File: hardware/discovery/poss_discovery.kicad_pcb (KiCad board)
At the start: 2 copper layers, 96.5 x 66 mm, 56 parts, among them J1 HEADER_2, J2 HEADER_25x2, J3 HEADER_25x2, J5 HEADER_2, SW1 SW_PUSH, SW10 SW_PUSH, SW11 SW_PUSH, SW12 SW_PUSH, SW13 SW_PUSH, SW14 SW_PUSH, SW15 SW_PUSH, SW16 SW_PUSH, SW17 SW_PUSH, SW18 SW_PUSH, SW19 SW_PUSH, SW2 SW_PUSH, SW20 SW_PUSH, SW21 SW_PUSH, SW22 SW_PUSH, SW3 SW_PUSH, SW4 SW_PUSH, SW5 SW_PUSH, SW6 SW_PUSH, SW7 SW_PUSH, SW8 SW_PUSH, SW9 SW_PUSH

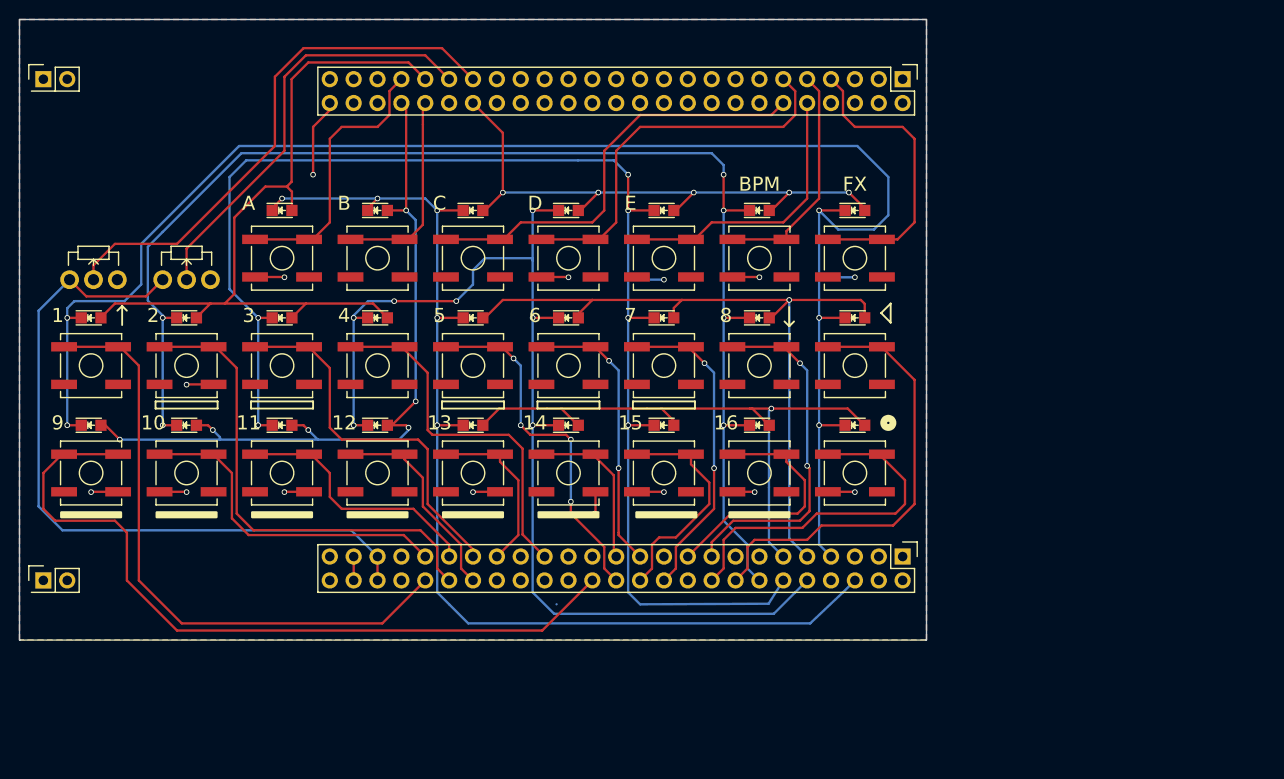
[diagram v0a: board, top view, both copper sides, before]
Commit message: Start RevB of the discovery board
- Fix RevA known problems
- Custom scheme and footprint for the headers
- Improved silkscreen
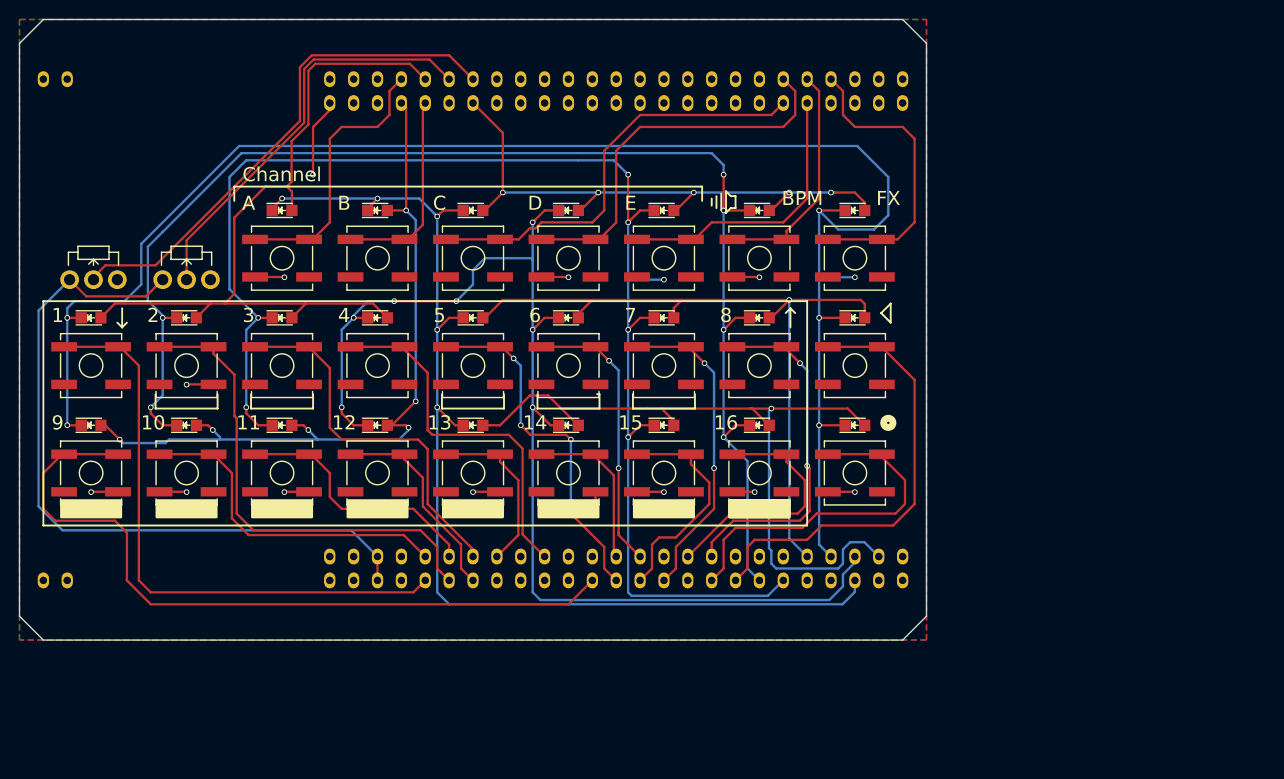
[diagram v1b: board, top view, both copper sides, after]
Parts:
- removed J1, J5: HEADER_2, Pin_Headers:Pin_Header_Straight_2x01
- removed J2, J3: HEADER_25x2, Pin_Headers:Pin_Header_Straight_2x25
- added U1: STM32F4_DISCO_Header, stm32f4-disco:STM32F4-DISCO-HEADERS-TH, B.Cu at (80.0, 95.2)
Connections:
- net /3V renamed 3V
- net /COL1 renamed COL1
- net /COL2 renamed COL2
- net /COL3 renamed COL3
- net /COL4 renamed COL4
- net /COL5 renamed COL5
- net /GND renamed GND
- net /PA13 renamed ROW2
- net /PA15 renamed ROW3
- net /PA8 renamed ROW5
- net /PC11 renamed ROW4
- net /PC9 renamed ROW1
- Play1 pad 1: /PD0 -> Play
- Play2 pad 1: /FX -> FX
- RV1 pad 2: /PA1 -> POT1
- RV2 pad 2: /PA3 -> POT2
- SW1 pad 1: /B1 -> B1
- SW10 pad 1: /B10 -> B10
- SW11 pad 1: /B11 -> B11
- SW12 pad 1: /B12 -> B12
- SW13 pad 1: /B13 -> B13
- SW14 pad 1: /B14 -> B14
- SW15 pad 1: /B15 -> B15
- SW16 pad 1: /B16 -> B16
- SW17 pad 1: /BF1 -> BA
- SW18 pad 1: /BF2 -> BB
- SW19 pad 1: /BF3 -> BC
- SW2 pad 1: /B2 -> B2
- SW20 pad 1: /BF4 -> BD
- SW21 pad 1: /BF5 -> BE
- SW22 pad 1: /BPM -> BPM_VOL
- SW3 pad 1: /B3 -> B3
- SW4 pad 1: /B4 -> B4
- SW5 pad 1: /B5 -> B5
- SW6 pad 1: /B6 -> B6
- SW7 pad 1: /B7 -> B7
- SW8 pad 1: /B8 -> B8
- SW9 pad 1: /B9 -> B9
- Write1 pad 1: /PD2 -> Write
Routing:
- net /B9: track 81.6 -> 0.00 mm
- net B9: track 0.00 -> 79.2 mm
- net /B1: track 65.9 -> 0.00 mm
- net B1: track 0.00 -> 63.2 mm
- net /PA3: track 57.2 -> 0.00 mm
- net POT2: track 0.00 -> 54.8 mm
- net /B2: track 51.5 -> 0.00 mm
- net B2: track 0.00 -> 51.4 mm
- net Play: track 0.00 -> 47.7 mm
- net /PD0: track 47.7 -> 0.00 mm
- net /BF3: track 45.6 -> 0.00 mm
- net /PA1: track 45.4 -> 0.00 mm
- net POT1: track 0.00 -> 44.3 mm
- net /BF4: track 41.3 -> 0.00 mm
- net B3: track 0.00 -> 40.3 mm
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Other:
- outline, holes or cut-outs redrawn
- board text added: "Channel"
- board text added: "RevB"

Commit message: Discovery: Start power section
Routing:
- net GND: track 42.0 -> 33.6 mm, vias 13 -> 12
- net ROW2: track 125.6 -> 124.2 mm
- net COL3: track 62.3 -> 63.5 mm
- net COL2: track 78.9 -> 79.6 mm

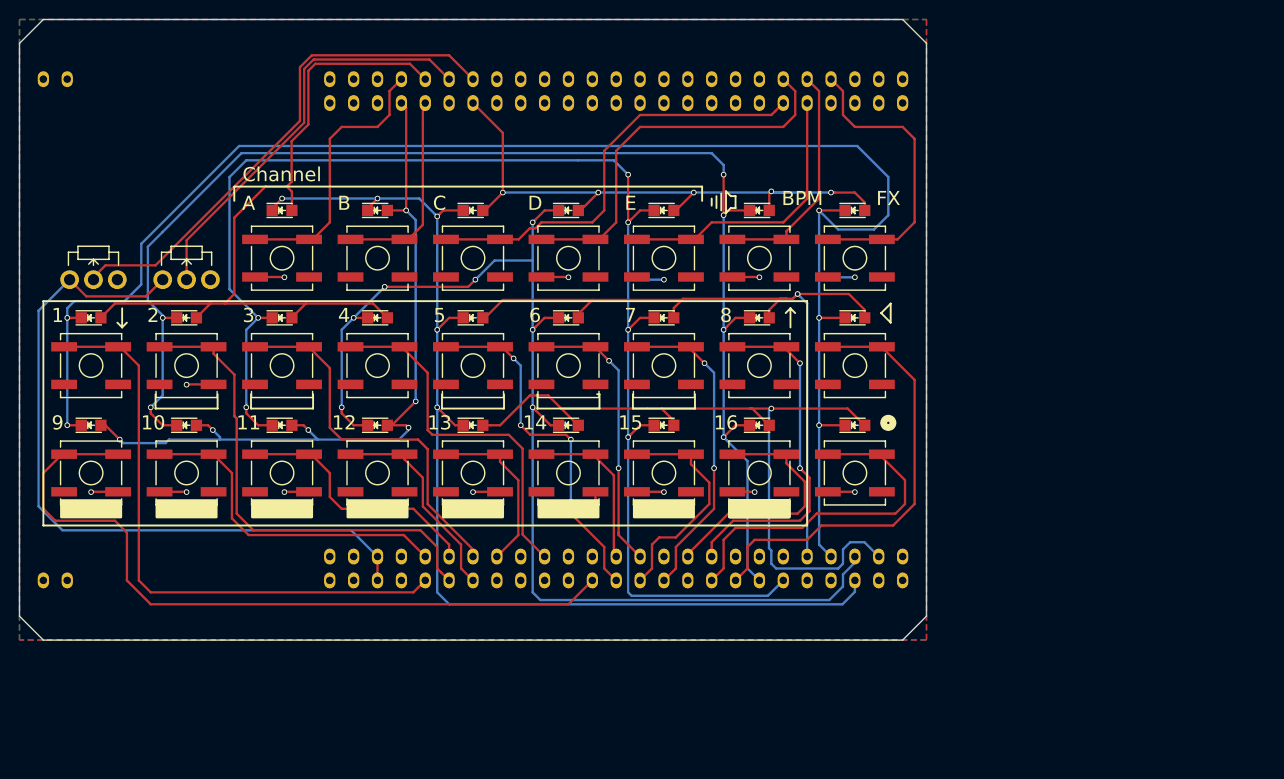
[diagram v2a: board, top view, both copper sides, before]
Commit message: Discovery: add the MCU
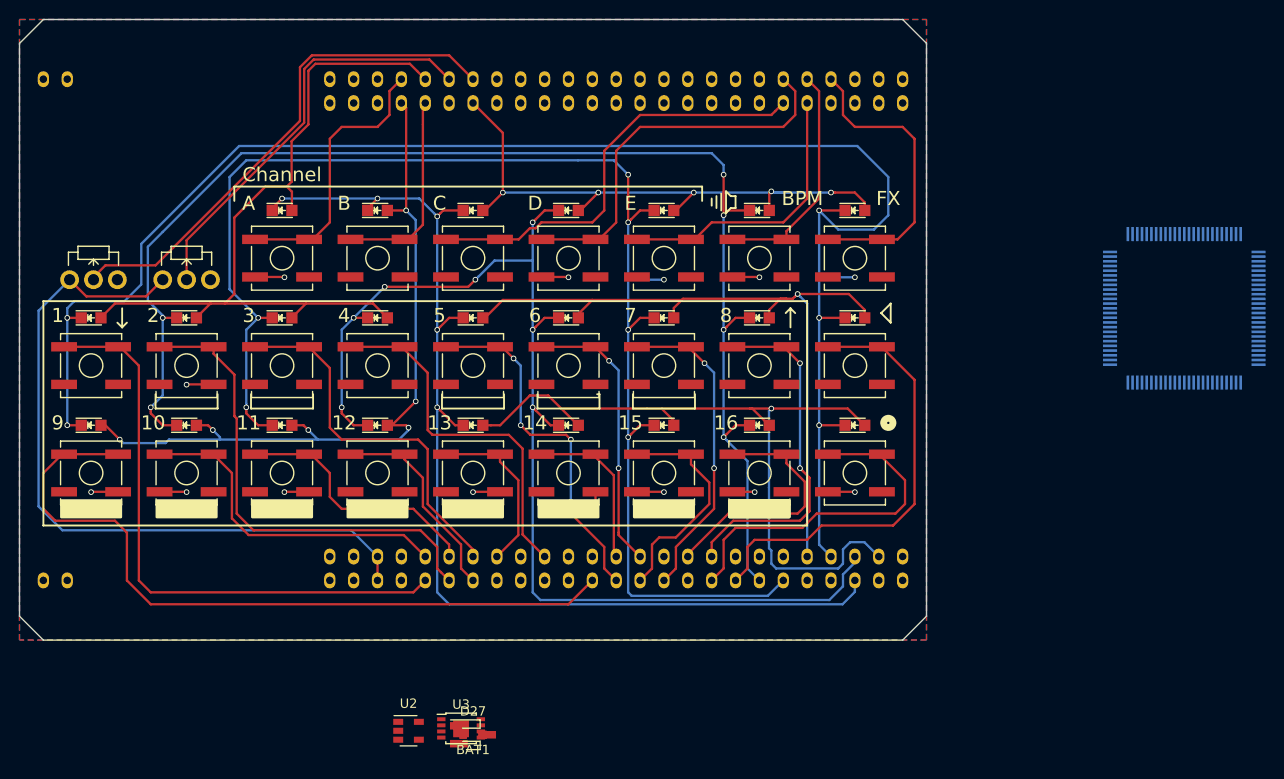
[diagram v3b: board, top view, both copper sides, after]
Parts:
- added BAT1: LED, Diodes_SMD:D_0805, F.Cu at (128.3, 154.9)
- added D27: DOUBLE_SCH_KCOM, TO_SOT_Packages_SMD:SOT-23_Handsoldering, F.Cu at (128.3, 154.9)
- added U2: MCP73831, TO_SOT_Packages_SMD:SOT-23-5, F.Cu at (121.4, 154.4)
- added U3: BD33IA5, Housings_SSOP:MSOP-8-1EP_3x3mm_Pitch0.65mm, F.Cu at (127.0, 154.2)
- added U4: STM32F407VG, Housings_QFP:LQFP-100_14x14mm_Pitch0.5mm, B.Cu at (204.0, 109.5)
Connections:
- net 3V renamed 3V3
- U1 pad 74: SWDCLK -> SWCLK

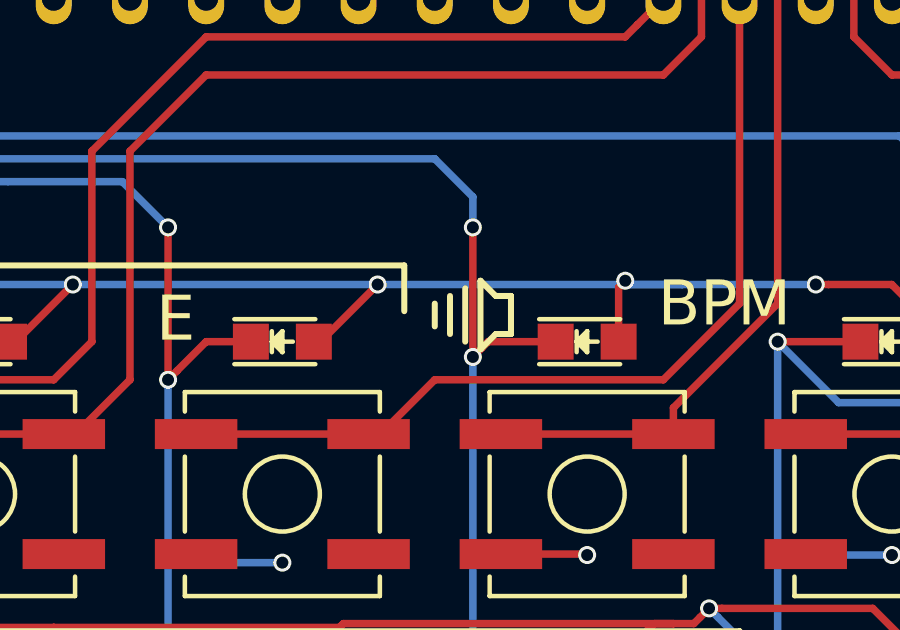
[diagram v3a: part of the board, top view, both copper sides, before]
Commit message: Discovery: Fix volume symbol
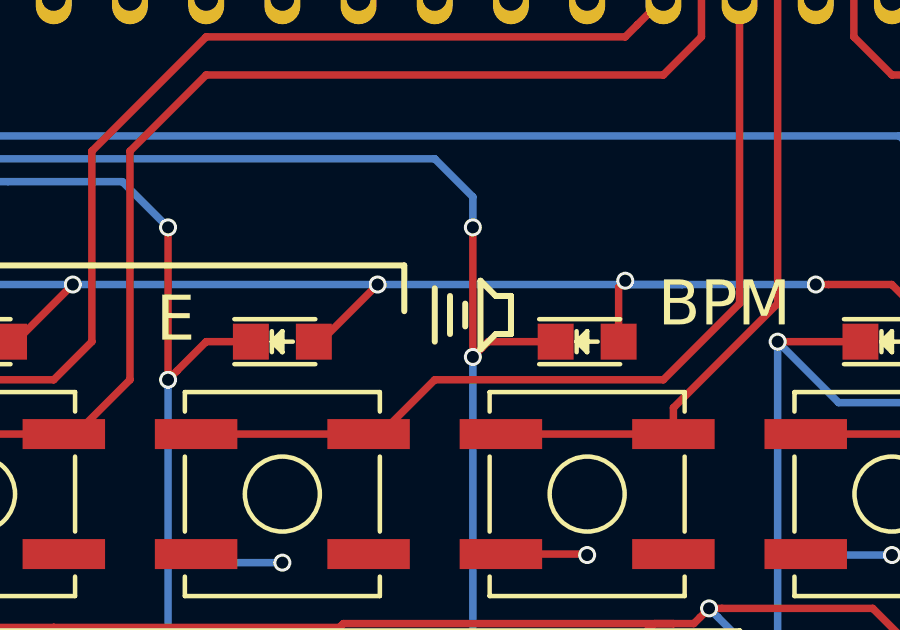
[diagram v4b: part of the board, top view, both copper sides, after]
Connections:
- U1 pad 22: BF4 -> BD
- U1 pad 32: BF2 -> BB
- U1 pad 47: BF3 -> BC
- U1 pad 48: BF5 -> BE
- U1 pad 6: BF1 -> BA
- U4 pad 16: BF1 -> BA
- U4 pad 17: BF2 -> BB
- U4 pad 54: BF4 -> BD
- U4 pad 55: BF3 -> BC
- U4 pad 57: BF5 -> BE
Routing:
- net BF3: track 37.9 -> 0.00 mm
- net BC: track 7.74 -> 45.6 mm
- net BF4: track 32.6 -> 0.00 mm
- net BD: track 8.70 -> 41.3 mm
- net BF5: track 21.4 -> 0.00 mm
- net BE: track 8.70 -> 30.1 mm
- net BF1: track 20.6 -> 0.00 mm
- net BA: track 8.70 -> 29.3 mm
- net BF2: track 13.1 -> 0.00 mm
- net BB: track 8.35 -> 21.4 mm

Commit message: Discovery start power section
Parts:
- added ?: tempo_logo, stm32f4-disco:tempo_logo, F.Cu at (162.1, 103.4)
- added BT1: BATTERY, Connect:PINHEAD1-2, F.Cu at (106.8, 83.9)
- added C1: 10uF, Capacitors_SMD:C_0805, F.Cu at (116.6, 81.4)
- added C2: 4.7uF, Capacitors_SMD:C_0805, F.Cu at (140.4, 83.2)
- added C3: 47uF, Capacitors_SMD:C_1206, F.Cu at (149.5, 83.3)
- added CON1: USB-MICRO-B, Connect:USB_Micro-B, F.Cu at (128.8, 83.3)
- added R1: 1K, Resistors_SMD:R_0805, F.Cu at (119.8, 84.3)
- added R2: 10K, Resistors_SMD:R_0805, F.Cu at (112.9, 84.5)
- D27: value DOUBLE_SCH_KCOM -> DOUBLE_SCH_KCOM_PMEG2005CT; footprint TO_SOT_Packages_SMD:SOT-23_Handsoldering -> TO_SOT_Packages_SMD:SOT-23
- U1: footprint stm32f4-disco:STM32F4-DISCO-HEADERS-TH -> stm32f4-disco:STM32F4-DISCO-HEADERS-SMD
- U4: moved to F.Cu
- moved U3 73.1 mm to (144.8, 83.2), turned to 180 degrees
- moved BAT1 71.0 mm to (121.8, 84.2), turned to 90 degrees
- moved U2 70.3 mm to (116.6, 84.3), turned to 180 degrees
- moved D27 66.8 mm to (128.8, 88.0), turned to 270 degrees
- moved U4 47.5 mm to (160.0, 91.4)
- moved U1 28.2 mm to (108.0, 91.4)
- moved D21 19.1 mm to (117.9, 118.1)
- moved D10 7.62 mm to (168.9, 118.1)
- moved D11 7.62 mm to (128.3, 106.7)
- moved D12 7.62 mm to (138.4, 106.7)
- moved D13 7.62 mm to (148.6, 106.7)
- moved D14 7.62 mm to (158.8, 106.7)
- moved D15 7.62 mm to (168.9, 106.7)
- moved D16 7.62 mm to (108.0, 106.7)
- moved D18 7.62 mm to (108.0, 118.1)
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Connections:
- D27 pad 1: VBAT -> VBUS
- D27 pad 2: VIN -> VBAT
- D27 pad 3: VBUS -> VIN
- U4 pad 70: Net-(U4-Pad70) -> FS_DM
- U4 pad 71: Net-(U4-Pad71) -> FS_DP
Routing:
- net ROW5: track 172.4 -> 0.00 mm, vias 5 -> 0
- net ROW3: track 147.8 -> 0.00 mm, vias 6 -> 0
- net ROW4: track 144.9 -> 0.00 mm, vias 6 -> 0
- net ROW2: track 124.2 -> 0.00 mm, vias 7 -> 0
- net ROW1: track 117.3 -> 0.00 mm, vias 5 -> 0
- net COL5: track 82.3 -> 0.00 mm, vias 6 -> 0
- net COL4: track 82.0 -> 0.00 mm
- net COL1: track 82.0 -> 0.00 mm, vias 1 -> 0
- net COL2: track 79.6 -> 0.00 mm, vias 1 -> 0
- net B9: track 79.2 -> 0.00 mm
- net 3V3: track 77.7 -> 3.63 mm
- net COL3: track 63.5 -> 0.00 mm, vias 5 -> 0
- net B1: track 63.2 -> 0.00 mm
- net POT2: track 54.8 -> 0.00 mm
- net B2: track 51.4 -> 0.00 mm
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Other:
- board text removed: "BPM"

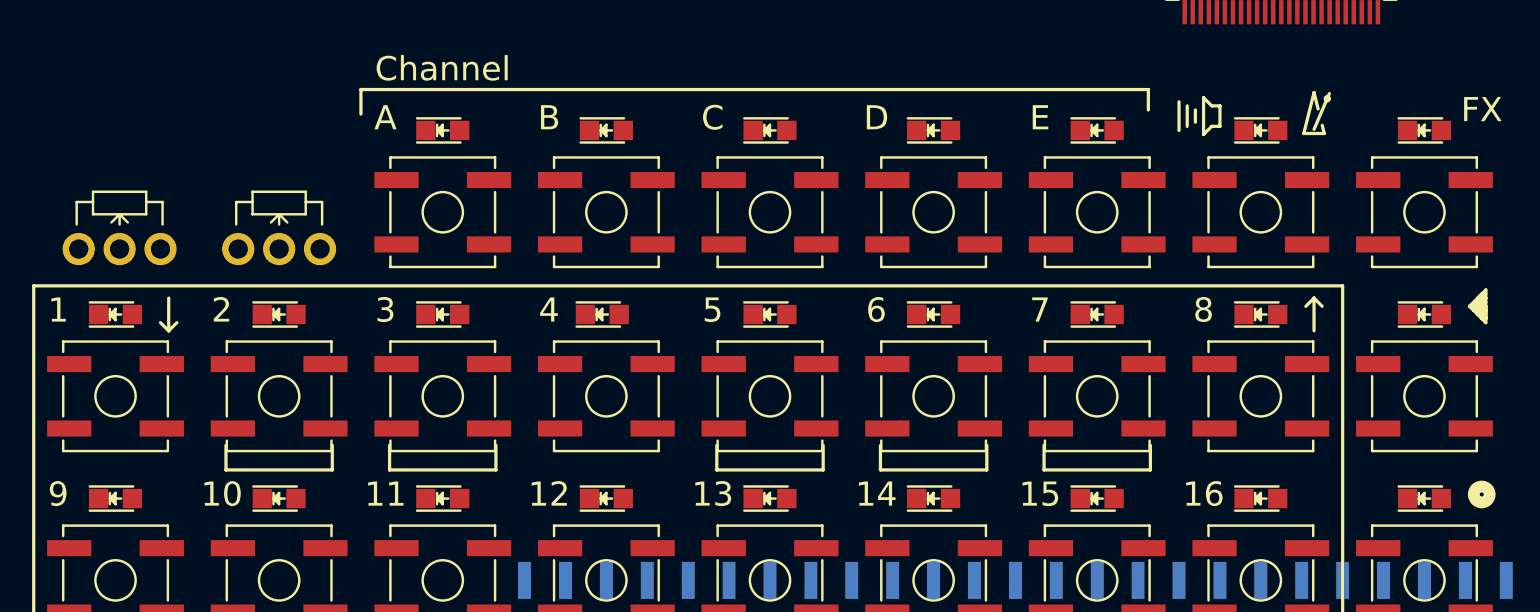
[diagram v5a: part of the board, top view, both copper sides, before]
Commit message: Discovery: switch to a 9x3 LED matrix to simplify the PCB layout
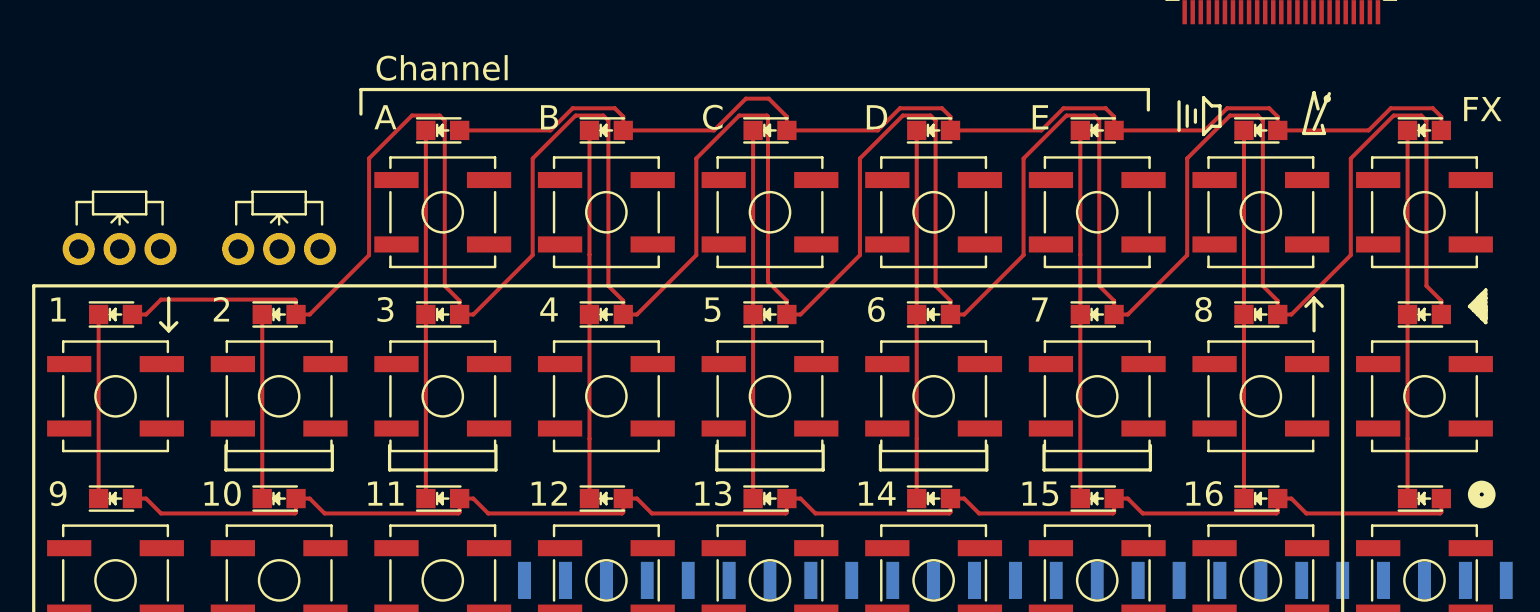
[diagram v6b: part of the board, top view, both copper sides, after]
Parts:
- moved D25 84.4 mm to (168.9, 106.7)
- moved D10 81.3 mm to (87.6, 118.1)
- moved D24 65.1 mm to (158.8, 106.7)
- moved D18 61.0 mm to (168.9, 118.1)
- moved D23 46.6 mm to (148.6, 106.7)
- moved D16 42.2 mm to (148.6, 118.1)
- moved D17 42.2 mm to (158.8, 118.1)
- moved D1 40.6 mm to (87.6, 129.5)
- moved D2 40.6 mm to (97.8, 129.5)
- moved D3 40.6 mm to (108.0, 129.5)
- moved D4 40.6 mm to (118.1, 129.5)
- moved D5 40.6 mm to (128.3, 129.5)
- moved D11 32.6 mm to (97.8, 118.1)
- moved D12 32.6 mm to (108.0, 118.1)
- moved D13 32.6 mm to (118.1, 118.1)
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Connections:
- D1 pad 1: ROW1 -> COL1
- D1 pad 2: COL1 -> ROW1
- D10 pad 1: ROW5 -> COL1
- D10 pad 2: COL2 -> ROW2
- D11 pad 1: ROW1 -> COL2
- D11 pad 2: COL3 -> ROW2
- D12 pad 1: ROW2 -> COL3
- D12 pad 2: COL3 -> ROW2
- D13 pad 1: ROW3 -> COL4
- D13 pad 2: COL3 -> ROW2
- D14 pad 1: ROW4 -> COL5
- D14 pad 2: COL3 -> ROW2
- D15 pad 1: ROW5 -> COL6
- D15 pad 2: COL3 -> ROW2
- D16 pad 1: ROW1 -> COL7
- D16 pad 2: COL4 -> ROW2
- D17 pad 1: ROW2 -> COL8
- D17 pad 2: COL4 -> ROW2
- D18 pad 1: ROW3 -> COL9
- D18 pad 2: COL4 -> ROW2
- D19 pad 1: ROW4 -> COL3
- D19 pad 2: COL4 -> ROW3
- D2 pad 1: ROW2 -> COL2
- D2 pad 2: COL1 -> ROW1
- D20 pad 1: ROW5 -> COL4
- D20 pad 2: COL4 -> ROW3
- D21 pad 1: ROW1 -> COL5
- D21 pad 2: COL5 -> ROW3
- D22 pad 1: ROW2 -> COL6
- D22 pad 2: COL5 -> ROW3
- D23 pad 1: ROW3 -> COL7
- D23 pad 2: COL5 -> ROW3
- D24 pad 1: ROW4 -> COL8
- D24 pad 2: COL5 -> ROW3
- D25 pad 1: ROW5 -> COL9
- D25 pad 2: COL5 -> ROW3
- D3 pad 1: ROW3 -> COL3
- D3 pad 2: COL1 -> ROW1
- D4 pad 1: ROW4 -> COL4
- D4 pad 2: COL1 -> ROW1
- D5 pad 1: ROW5 -> COL5
- D5 pad 2: COL1 -> ROW1
- D6 pad 1: ROW1 -> COL6
- D6 pad 2: COL2 -> ROW1
- D7 pad 1: ROW2 -> COL7
- D7 pad 2: COL2 -> ROW1
- D8 pad 1: ROW3 -> COL8
- D8 pad 2: COL2 -> ROW1
- D9 pad 1: ROW4 -> COL9
- D9 pad 2: COL2 -> ROW1
- U1 pad 21: Net-(U1-Pad21) -> COL9
- U1 pad 46: Net-(U1-Pad46) -> COL8
- U1 pad 76: ROW5 -> COL6
- U1 pad 98: ROW4 -> COL7
- U4 pad 67: ROW5 -> ROw5
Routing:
- net ROW2: track 0.00 -> 224.4 mm
- net ROW1: track 0.00 -> 91.4 mm
- net ROW3: track 0.00 -> 71.3 mm
- net COL9: track 0.00 -> 22.9 mm
- net COL8: track 0.00 -> 22.9 mm
- net COL7: track 0.00 -> 22.9 mm
- net COL6: track 0.00 -> 22.9 mm
- net COL5: track 0.00 -> 22.9 mm
- net COL4: track 0.00 -> 22.9 mm
- net COL3: track 0.00 -> 22.9 mm
- net COL2: track 0.00 -> 11.4 mm
- net COL1: track 0.00 -> 11.4 mm
